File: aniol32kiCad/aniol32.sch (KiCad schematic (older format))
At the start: 16 parts, among them SW1 RESET, U2 74HC14, U5 Z80CPU

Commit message: Introduced hierarchical design in KiCad
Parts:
- removed U?: 74LS32, symbol 74xx:74LS32
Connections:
- net labels removed: DARTSEL
- wire segments 77 -> 75
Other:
- moved on the sheet: C1, R10
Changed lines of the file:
@@
 $Descr A4 11693 8268
 encoding utf-8
-Sheet 1 3
+Sheet 1 5
 Title ""
 Date ""
@@
 RD
 Wire Wire Line
-	10300 5950 10150 5950
-Connection ~ 10150 5950
+	1400 5350 1250 5350
+Connection ~ 1250 5350
 $Comp
 L Switch:SW_SPST SW1
 U 1 1 6165D2A8
-P 9750 5700
-F 0 "SW1" V 9650 5450 50  0000 L CNN
-F 1 "RESET" V 9750 5400 50  0000 L CNN
-F 2 "Button_Switch_THT:KSA_Tactile_SPST" H 9750 5700 50  0001 C CNN
-F 3 "~" H 9750 5700 50  0001 C CNN
-	1    9750 5700
+P 850 5100
+F 0 "SW1" V 750 4850 50  0000 L CNN
+F 1 "RESET" V 850 4800 50  0000 L CNN
+F 2 "Button_Switch_THT:KSA_Tactile_SPST" H 850 5100 50  0001 C CNN
+F 3 "~" H 850 5100 50  0001 C CNN
+	1    850  5100
 	0    1    1    0
 $EndComp
@@
 L power:GND #PWR04
 U 1 1 61665C17
-P 10150 6250
-F 0 "#PWR04" H 10150 6000 50  0001 C CNN
-F 1 "GND" H 10155 6077 50  0000 C CNN
-F 2 "" H 10150 6250 50  0001 C CNN
-F 3 "" H 10150 6250 50  0001 C CNN
-	1    10150 6250
+P 1250 5650
+F 0 "#PWR04" H 1250 5400 50  0001 C CNN
+F 1 "GND" H 1255 5477 50  0000 C CNN
+F 2 "" H 1250 5650 50  0001 C CNN
+F 3 "" H 1250 5650 50  0001 C CNN
+	1    1250 5650
 	1    0    0    -1
 $EndComp
@@
 L pspice:C C1
 U 1 1 61643998
-P 10150 5700
-F 0 "C1" H 10328 5746 50  0000 L CNN
-F 1 "1n" H 10328 5655 50  0000 L CNN
-F 2 "Capacitor_THT:CP_Radial_D8.0mm_P5.00mm" H 10150 5700 50  0001 C CNN
-F 3 "~" H 10150 5700 50  0001 C CNN
-	1    10150 5700
+P 1250 5100
+F 0 "C1" H 1428 5146 50  0000 L CNN
+F 1 "1n" H 1428 5055 50  0000 L CNN
+F 2 "Capacitor_THT:CP_Radial_D8.0mm_P5.00mm" H 1250 5100 50  0001 C CNN
+F 3 "~" H 1250 5100 50  0001 C CNN
+	1    1250 5100
 	1    0    0    -1
 $EndComp
@@
 L Device:R R10
 U 1 1 61642F4B
-P 10150 6100
-F 0 "R10" H 10220 6146 50  0000 L CNN
-F 1 "1k" H 10220 6055 50  0000 L CNN
-F 2 "Resistor_THT:R_Axial_DIN0207_L6.3mm_D2.5mm_P7.62mm_Horizontal" V 10080 6100 50  0001 C CNN
-F 3 "~" H 10150 6100 50  0001 C CNN
-	1    10150 6100
+P 1250 5500
+F 0 "R10" H 1320 5546 50  0000 L CNN
+F 1 "1k" H 1320 5455 50  0000 L CNN
+F 2 "Resistor_THT:R_Axial_DIN0207_L6.3mm_D2.5mm_P7.62mm_Horizontal" V 1180 5500 50  0001 C CNN
+F 3 "~" H 1250 5500 50  0001 C CNN
+	1    1250 5500
 	1    0    0    -1
 $EndComp
 Text GLabel 6950 1600 0    50   Input ~ 0
 RST
-Text GLabel 10900 5950 2    50   Input ~ 0
+Text GLabel 2000 5350 2    50   Input ~ 0
 RST
 Wire Wire Line
-	10150 5450 10150 5400
-Wire Wire Line
-	9750 5500 9750 5450
-Wire Wire Line
-	9750 5450 10150 5450
-Connection ~ 10150 5450
-Wire Wire Line
-	9750 5950 9750 5900
-Wire Wire Line
-	9750 5950 10150 5950
+	1250 4850 1250 4800
+Wire Wire Line
+	850  4900 850  4850
+Wire Wire Line
+	850  4850 1250 4850
+Connection ~ 1250 4850
+Wire Wire Line
+	850  5350 850  5300
+Wire Wire Line
+	850  5350 1250 5350
 Text GLabel 6950 1900 0    50   Input ~ 0
 CLK
@@
 L 74xx:74HC14 U2
 U 3 1 61971392
-P 10600 5950
-F 0 "U2" H 10600 6267 50  0000 C CNN
-F 1 "74HC14" H 10600 6176 50  0000 C CNN
-F 2 "Package_DIP:DIP-14_W7.62mm" H 10600 5950 50  0001 C CNN
-F 3 "http://www.ti.com/lit/gpn/sn74HC14" H 10600 5950 50  0001 C CNN
-	3    10600 5950
+P 1700 5350
+F 0 "U2" H 1700 5667 50  0000 C CNN
+F 1 "74HC14" H 1700 5576 50  0000 C CNN
+F 2 "Package_DIP:DIP-14_W7.62mm" H 1700 5350 50  0001 C CNN
+F 3 "http://www.ti.com/lit/gpn/sn74HC14" H 1700 5350 50  0001 C CNN
+	3    1700 5350
 	1    0    0    -1
 $EndComp
@@
 L power:+5V #PWR?
 U 1 1 61A9FBC3
-P 10150 5400
-F 0 "#PWR?" H 10150 5250 50  0001 C CNN
-F 1 "+5V" H 10165 5573 50  0000 C CNN
-F 2 "" H 10150 5400 50  0001 C CNN
-F 3 "" H 10150 5400 50  0001 C CNN
-	1    10150 5400
+P 1250 4800
+F 0 "#PWR?" H 1250 4650 50  0001 C CNN
+F 1 "+5V" H 1265 4973 50  0000 C CNN
+F 2 "" H 1250 4800 50  0001 C CNN
+F 3 "" H 1250 4800 50  0001 C CNN
+	1    1250 4800
 	1    0    0    -1
 $EndComp
@@
 Wire Bus Line
 	9750 650  11000 650
-Wire Wire Line
-	1750 1200 1000 1200
-Text GLabel 1000 1200 0    50   Input ~ 0
-A4
-Wire Wire Line
-	1750 1000 1000 1000
-Text GLabel 1000 1000 0    50   Input ~ 0
-IORQ
-Text GLabel 2350 1100 2    50   Input ~ 0
-DARTSEL
-$Comp
-L 74xx:74LS32 U?
-U 4 1 61834289
-P 2050 1100
-F 0 "U?" H 2050 1425 50  0000 C CNN
-F 1 "74LS32" H 2050 1334 50  0000 C CNN
-F 2 "" H 2050 1100 50  0001 C CNN
-F 3 "http://www.ti.com/lit/gpn/sn74LS32" H 2050 1100 50  0001 C CNN
-	4    2050 1100
-	1    0    0    -1
-$EndComp
 NoConn ~ 8350 3100
 NoConn ~ 6950 4000
@@
 S 1200 1900 500  150
 U 61AEA36E
-F0 "Sheet61AEA36D" 50
+F0 "keyboard" 50
 F1 "Kbd.sch" 50
 $EndSheet
 $Sheet
-S 1250 2200 500  150
+S 1200 2300 500  150
 U 61ACCEA5
-F0 "Sheet61ACCEA4" 50
+F0 "HD44780 LCD" 50
 F1 "LCD.sch" 50
 $EndSheet
 Wire Wire Line
 	3100 7550 4600 7550
+$Sheet
+S 1200 2800 500  150
+U 618A74E4
+F0 "Z80DART" 50
+F1 "DART.sch" 50
+$EndSheet
 Wire Bus Line
 	11000 650  11000 4700
@@
 Wire Bus Line
 	8500 650  8500 3900
+$Sheet
+S 1200 3250 500  150
+U 618B3490
+F0 "expansion port" 50
+F1 "exp.sch" 50
+$EndSheet
 $EndSCHEMATC

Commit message: filling in the schematic
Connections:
- wire segments 75 -> 41
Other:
- moved on the sheet: R11, R12, R13, R14, U5, U?

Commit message: lots of changes
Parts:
- removed C1: 1n, Capacitor_THT:CP_Radial_D8.0mm_P5.00mm, symbol pspice:C
- removed C? (x2): 100n, symbol Device:C
- removed R10, R12: 1k, Resistor_THT:R_Axial_DIN0207_L6.3mm_D2.5mm_P7.62mm_Horizontal, symbol Device:R
- removed SW1: RESET, Button_Switch_THT:KSA_Tactile_SPST, symbol Switch:SW_SPST
- removed U2: 74HC14, Package_DIP:DIP-14_W7.62mm, symbol 74xx:74HC14
- added C10, C11, C12, C13, C14, C2, C3, C4, C5, C6, C7, C8, C9: 100n, Capacitor_THT:C_Disc_D5.0mm_W2.5mm_P5.00mm, symbol Device:C_Small
- added EXP_PORT1: Conn_01x24_Male, Connector_PinHeader_2.54mm:PinHeader_1x24_P2.54mm_Horizontal, symbol Connector:Conn_01x24_Male
- added J1: RST, Connector_PinHeader_2.54mm:PinHeader_1x02_P2.54mm_Vertical, symbol Connector:Conn_01x02_Male
- added J2: PWR, Connector_PinHeader_2.54mm:PinHeader_1x02_P2.54mm_Vertical, symbol Connector:Conn_01x02_Male
- added R1, R2: 4k7, Resistor_THT:R_Axial_DIN0207_L6.3mm_D2.5mm_P7.62mm_Horizontal, symbol Device:R_Small
- added SERIAL1: Conn_02x08_Counter_Clockwise, Connector_PinSocket_2.54mm:PinSocket_2x08_P2.54mm_Horizontal, symbol Connector_Generic:Conn_02x08_Counter_Clockwise
- added unit 1 of U1
- added unit 2 of U1
- added U12: 74LS74, Package_DIP:DIP-14_W7.62mm_Socket, symbol 74xx:74LS74
- added U2, U3: 74LS14, Package_DIP:DIP-14_W7.62mm_Socket, symbol 74xx:74LS14
- added U5: 74LS08, Package_DIP:DIP-14_W7.62mm_Socket, symbol 74xx:74LS08
- added U8: KM62256CLP, Package_DIP:DIP-28_W15.24mm_Socket, symbol Memory_RAM:KM62256CLP
- added U9: DART-DIP-40, Package_DIP:DIP-40_W15.24mm_Socket, symbol Zilog_Z80_Peripherals:DART-DIP-40
- added X1: ACO-1.8432MHz, Oscillator:Oscillator_DIP-14, symbol Oscillator:ACO-xxxMHz
- C1: renamed from C?; footprint (none) -> Capacitor_THT:CP_Radial_D14.0mm_P7.50mm
- U1, U4: renamed from U?; footprint (none) -> Package_DIP:DIP-14_W7.62mm_Socket
- U6: renamed from U5; footprint Package_DIP:DIP-40_W15.24mm -> Package_DIP:DIP-40_W15.24mm_Socket
- U7: renamed from U?; footprint (none) -> Package_DIP:DIP-28_W15.24mm_Socket
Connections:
- net labels added: A15, INT, KIE, NMI, RAMSEL, ROMSEL
- wire segments 41 -> 110
- no-connect marks 3 -> 18
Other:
- moved on the sheet: U4E

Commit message: tidying up the schematic
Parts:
- CPU1: renamed from U6; value Z80CPU -> Z80
- R11: value 1k -> 4k7
- SERIAL1: value Conn_02x08_Counter_Clockwise -> Conn_02x08
- U9: value DART-DIP-40 -> DART
- renumbered U8 to RAM1, U7 to ROM1
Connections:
- net +5V: now also SERIAL1.8 (Pin_8); no longer SERIAL1.16 (Pin_16)
- net CLK: now also SERIAL1.7 (Pin_7); no longer SERIAL1.9 (Pin_9)
- net GND: now also CPU1.29 (GND), SERIAL1.16 (Pin_16); no longer SERIAL1.8 (Pin_8)
- net NMI: now also CPU1.17 (~NMI~), R11.1
- net at U9.10 (~W~/~RDYA): now also SERIAL1.6 (Pin_6)
- net at U9.11 (~SYNCA): now also SERIAL1.5 (Pin_5)
- net at U9.12 (RXDA): now also SERIAL1.2 (Pin_2)
- net at U9.13 (~RXCA): now also SERIAL1.3 (Pin_3), U9.14 (~TXCA)
- net at U9.15 (TXDA): now also SERIAL1.4 (Pin_4)
- net at U9.22 (~DCDB): now also SERIAL1.1 (Pin_1); no longer SERIAL1.10 (Pin_10)
- net at U9.23 (~CTSB): now also SERIAL1.14 (Pin_14); no longer SERIAL1.6 (Pin_6)
- net at U9.24 (~RTSB): now also SERIAL1.13 (Pin_13); no longer SERIAL1.5 (Pin_5)
- net at U9.25 (~DTRB): now also SERIAL1.15 (Pin_15); no longer SERIAL1.7 (Pin_7)
- net at U9.26 (TXDB): now also SERIAL1.10 (Pin_10); no longer SERIAL1.2 (Pin_2)
- net at U9.28 (RXDB): now also SERIAL1.9 (Pin_9); no longer SERIAL1.1 (Pin_1)
- net at U9.29 (~SYNCB): now also SERIAL1.11 (Pin_11); no longer SERIAL1.3 (Pin_3)
- net at U9.30 (~W~/~RDYB): now also SERIAL1.12 (Pin_12); no longer SERIAL1.4 (Pin_4)
- no-connect marks 18 -> 8
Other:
- moved on the sheet: J2, R11, R13, R14, SERIAL1

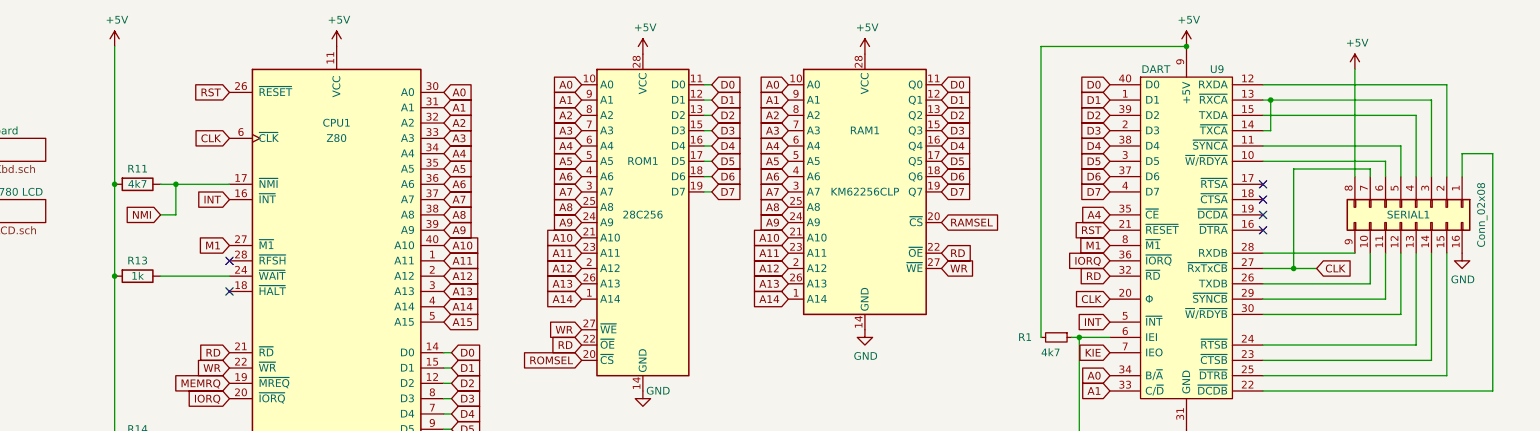
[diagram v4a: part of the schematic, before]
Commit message: created cal.asm, parsing is working for single-byte hex numbers, 5 operations and brackets
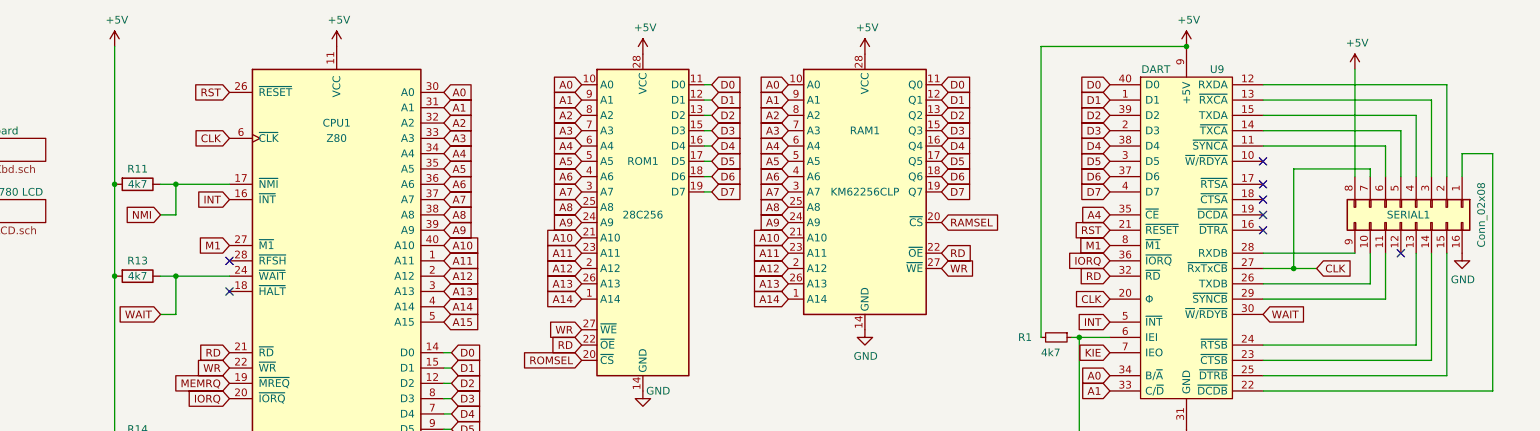
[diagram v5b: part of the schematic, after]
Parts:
- R13: value 1k -> 4k7
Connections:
- net WAIT: now reaches CPU1.24 (~WAIT~), R13.1
- net WAIT: now also U9.30 (~W~/~RDYB)
- net at U9.10 (~W~/~RDYA): no longer SERIAL1.6 (Pin_6)
- net at U9.11 (~SYNCA): now also SERIAL1.6 (Pin_6); no longer SERIAL1.5 (Pin_5)
- net at SERIAL1.3 (Pin_3), U9.13 (~RXCA): no longer U9.14 (~TXCA)
- net at SERIAL1.12 (Pin_12): no longer U9.30 (~W~/~RDYB)
- new net: SERIAL1.5 (Pin_5), U9.14 (~TXCA)
- no-connect marks 8 -> 10
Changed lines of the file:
@@
 P 2300 2800
 F 0 "R13" V 2200 2800 50  0000 C CNN
-F 1 "1k" V 2300 2800 50  0000 C CNN
+F 1 "4k7" V 2300 2800 50  0000 C CNN
 F 2 "Resistor_THT:R_Axial_DIN0207_L6.3mm_D2.5mm_P7.62mm_Horizontal" V 2230 2800 50  0001 C CNN
 F 3 "~" H 2300 2800 50  0001 C CNN
@@
 NoConn ~ 9650 2400
 NoConn ~ 9650 2500
-Wire Wire Line
-	9650 1850 9700 1850
-Wire Wire Line
-	9700 1850 9700 1650
-Wire Wire Line
-	9700 1650 9650 1650
 $Comp
 L Connector_Generic:Conn_02x08_Counter_Clockwise SERIAL1
@@
 	9650 2950 10450 2950
 Wire Wire Line
-	9650 3050 10550 3050
-Wire Wire Line
 	9650 3250 10650 3250
 Wire Wire Line
@@
 	9650 1550 10850 1550
 Wire Wire Line
-	9700 1650 10750 1650
-Connection ~ 9700 1650
-Wire Wire Line
 	9650 1750 10650 1750
 Wire Wire Line
-	9650 1950 10550 1950
-Wire Wire Line
 	10350 2850 10350 2650
 Wire Wire Line
 	10450 2950 10450 2650
 Wire Wire Line
-	10550 3050 10550 2650
-Wire Wire Line
 	10650 3250 10650 2650
 Wire Wire Line
@@
 Wire Wire Line
 	10650 1750 10650 2150
-Wire Wire Line
-	10550 1950 10550 2150
-Wire Wire Line
-	9650 2050 10450 2050
-Wire Wire Line
-	10450 2050 10450 2150
 Wire Wire Line
 	10350 2150 10350 2100
@@
 	2900 2200 2550 2200
 Wire Wire Line
-	2900 2800 2450 2800
+	2900 2800 2550 2800
 Wire Wire Line
 	2900 3900 2450 3900
@@
 Wire Wire Line
 	1150 7550 850  7550
+Wire Wire Line
+	9650 1650 10750 1650
+Wire Wire Line
+	10550 1850 10550 2150
+Wire Wire Line
+	9650 1850 10550 1850
+Wire Wire Line
+	9650 1950 10450 1950
+Wire Wire Line
+	10450 1950 10450 2150
+Text GLabel 2450 3050 0    50   Input ~ 0
+WAIT
+Wire Wire Line
+	2450 3050 2550 3050
+Wire Wire Line
+	2550 3050 2550 2800
+Connection ~ 2550 2800
+Wire Wire Line
+	2550 2800 2450 2800
+Text GLabel 9650 3050 2    50   Input ~ 0
+WAIT
+NoConn ~ 10550 2650
+NoConn ~ 9650 2050
 $EndSCHEMATC

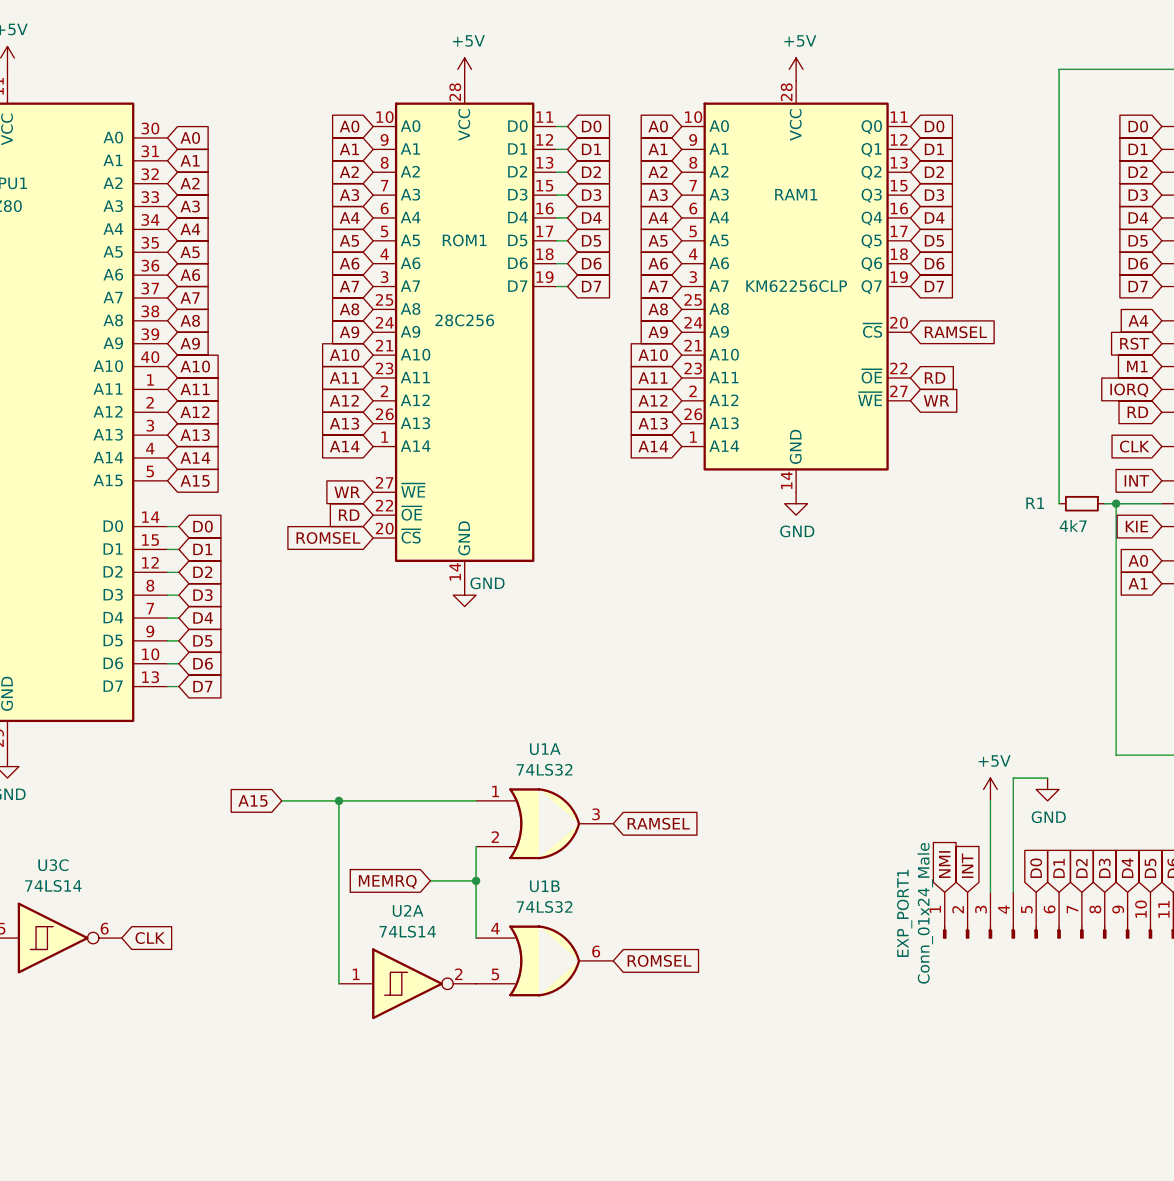
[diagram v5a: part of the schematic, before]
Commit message: added bitmapped text bin file generator
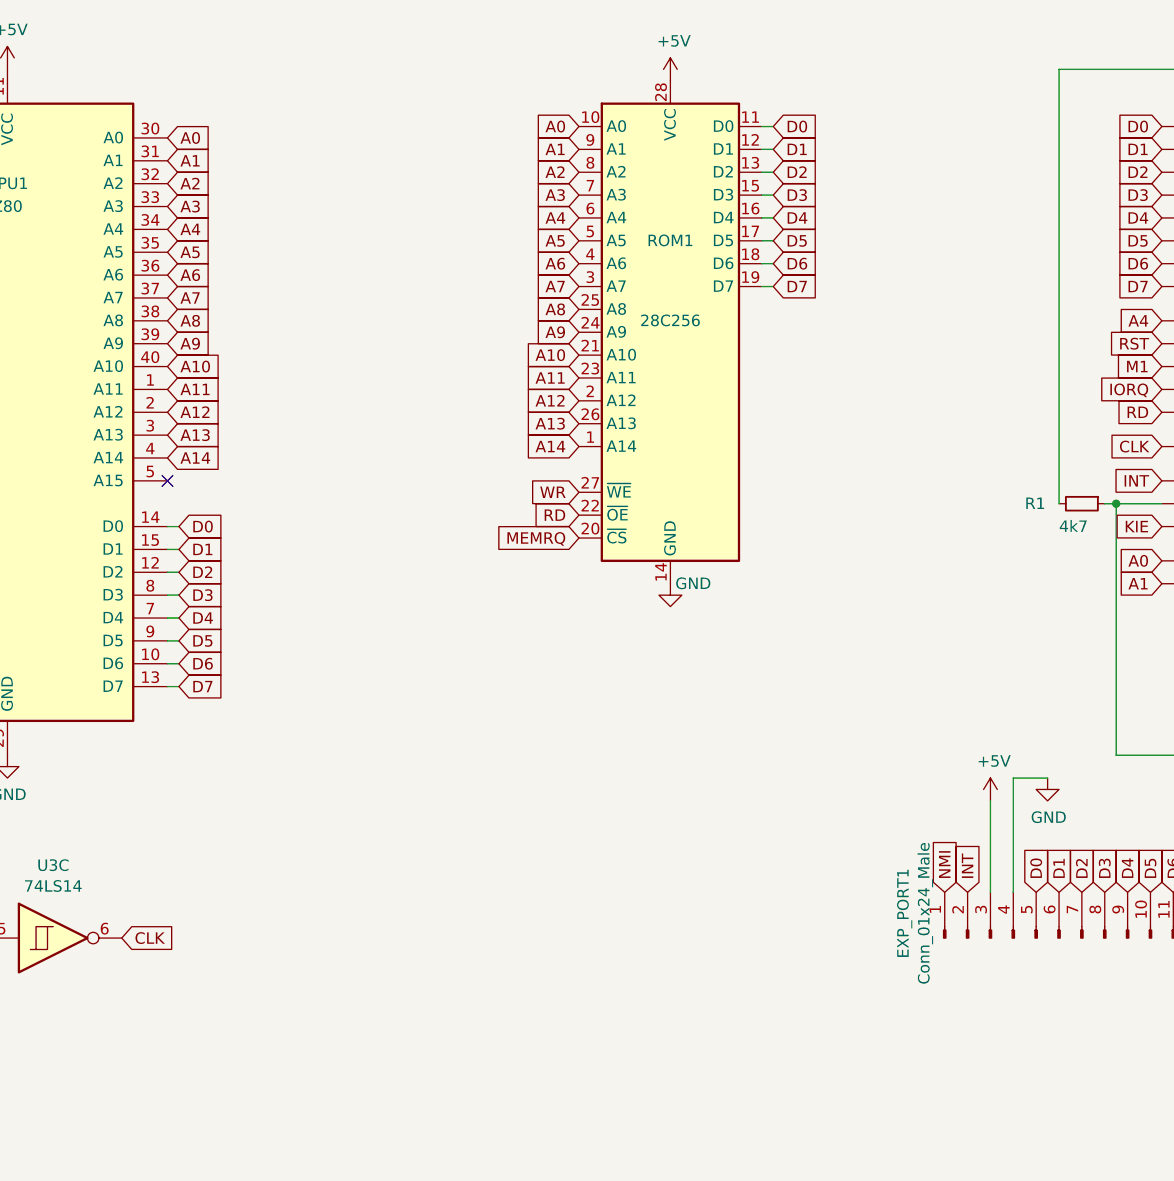
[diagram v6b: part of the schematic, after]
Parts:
- removed RAM1: KM62256CLP, Package_DIP:DIP-28_W15.24mm_Socket, symbol Memory_RAM:KM62256CLP
- removed unit 1 of U1
- removed unit 2 of U1
- removed unit 1 of U2
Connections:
- net ROMSEL is gone; now on net MEMRQ: ROM1.20 (~CS)
- net A15: no longer names the net of CPU1.5 (A15)
- no-connect marks 10 -> 11
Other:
- moved on the sheet: ROM1

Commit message: tidied up the PCB
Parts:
- removed SERIAL1: Conn_02x08, Connector_PinSocket_2.54mm:PinSocket_2x08_P2.54mm_Horizontal, symbol Connector_Generic:Conn_02x08_Counter_Clockwise
- added J3: Conn_02x08_Odd_Even, Connector_PinSocket_2.54mm:PinSocket_2x08_P2.54mm_Horizontal, symbol Connector_Generic:Conn_02x08_Odd_Even
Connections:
- net +5V: now also J3.15 (Pin_15)
- net CLK: now also J3.13 (Pin_13)
- net GND: now also J3.2 (Pin_2)
- net at U9.11 (~SYNCA): now also J3.11 (Pin_11)
- net at U9.12 (RXDA): now also J3.3 (Pin_3)
- net at U9.13 (~RXCA): now also J3.5 (Pin_5)
- net at U9.14 (~TXCA): now also J3.9 (Pin_9)
- net at U9.15 (TXDA): now also J3.7 (Pin_7)
- net at U9.22 (~DCDB): now also J3.1 (Pin_1)
- net at U9.23 (~CTSB): now also J3.6 (Pin_6)
- net at U9.24 (~RTSB): now also J3.8 (Pin_8)
- net at U9.25 (~DTRB): now also J3.4 (Pin_4)
- net at U9.26 (TXDB): now also J3.14 (Pin_14)
- net at U9.28 (RXDB): now also J3.16 (Pin_16)
- net at U9.29 (~SYNCB): now also J3.12 (Pin_12)
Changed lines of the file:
@@
 NoConn ~ 9650 2400
 NoConn ~ 9650 2500
-$Comp
-L Connector_Generic:Conn_02x08_Counter_Clockwise SERIAL1
-U 1 1 61CEB7DC
-P 10650 2350
-F 0 "SERIAL1" V 10700 2300 50  0000 C CNN
-F 1 "Conn_02x08" H 10700 2776 50  0000 C CNN
-F 2 "Connector_PinSocket_2.54mm:PinSocket_2x08_P2.54mm_Horizontal" H 10650 2350 50  0001 C CNN
-F 3 "~" H 10650 2350 50  0001 C CNN
-	1    10650 2350
-	0    1    1    0
-$EndComp
 Wire Wire Line
 	9650 2850 10350 2850
@@
 MEMRQ
 NoConn ~ 4300 3100
+$Comp
+L Connector_Generic:Conn_02x08_Odd_Even J3
+U 1 1 621728BB
+P 10650 2350
+F 0 "J3" V 10654 2730 50  0000 L CNN
+F 1 "Conn_02x08_Odd_Even" V 10745 2730 50  0000 L CNN
+F 2 "Connector_PinSocket_2.54mm:PinSocket_2x08_P2.54mm_Horizontal" H 10650 2350 50  0001 C CNN
+F 3 "~" H 10650 2350 50  0001 C CNN
+	1    10650 2350
+	0    1    1    0
+$EndComp
 $EndSCHEMATC
